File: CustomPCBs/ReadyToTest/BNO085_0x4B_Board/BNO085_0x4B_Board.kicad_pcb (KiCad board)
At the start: 4 copper layers, 8.1 x 8.8 mm, 12 parts, among them J1 Conn_01x04_Pin, Y1 32.768kHz

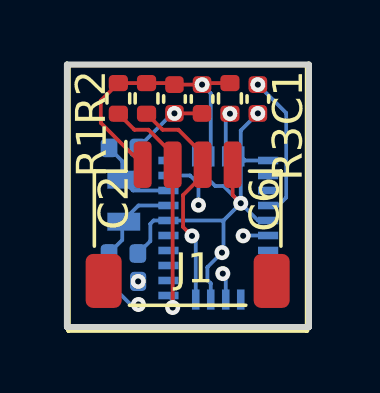
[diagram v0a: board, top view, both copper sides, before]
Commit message: Updating IMU boards for different wire connections
Now all components are placed on one layer, making assembly easier. The
JST connector was dropped for smalled IMU housing, instead the wires now
solder directly to the board and exit from the sides of the board.
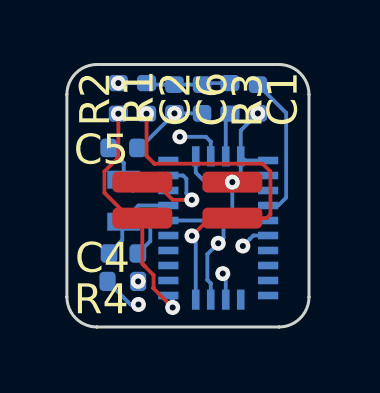
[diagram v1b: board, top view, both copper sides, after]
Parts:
- C1, C2, C6, R1, R2, R3: moved to B.Cu
- J1: footprint Connector_JST:JST_SH_SM04B-SRSS-TB_1x04-1MP_P1.00mm_Horizontal -> Library:WireToBoard2x2Wide
- moved J1 0.82 mm to (98.3, 109.5)
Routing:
- net SCL: track 7.73 -> 12.4 mm, vias 1 -> 2
- net +3V3: track 11.6 -> 8.67 mm, vias 3 -> 4
- net GND: track 20.0 -> 18.5 mm
- net SDA: track 7.94 -> 8.31 mm, vias 1 -> 2
- net Net-(U1-CAP): vias 1 -> 0
- net Net-(U1-BOOTN): vias 1 -> 0
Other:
- outline, holes or cut-outs redrawn
